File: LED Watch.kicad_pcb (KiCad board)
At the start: 2 copper layers, 41.9 x 49.3 mm, 140 parts, among them J1 AVR-ISP-6, J2 Lipo, J3 Coin Cell, SW1 SW_DPST, SW2 SW_DPST, U10 B39D3RGB-F6C0001HOU1930, U100 B39D3RGB-F6C0001HOU1930, U101 B39D3RGB-F6C0001HOU1930, U102 B39D3RGB-F6C0001HOU1930, U103 B39D3RGB-F6C0001HOU1930, U104 B39D3RGB-F6C0001HOU1930, U105 B39D3RGB-F6C0001HOU1930, U106 B39D3RGB-F6C0001HOU1930, U107 B39D3RGB-F6C0001HOU1930, U108 B39D3RGB-F6C0001HOU1930, U109 B39D3RGB-F6C0001HOU1930, U11 B39D3RGB-F6C0001HOU1930, U110 B39D3RGB-F6C0001HOU1930, U111 B39D3RGB-F6C0001HOU1930, U112 B39D3RGB-F6C0001HOU1930, U113 B39D3RGB-F6C0001HOU1930, U114 B39D3RGB-F6C0001HOU1930, U115 B39D3RGB-F6C0001HOU1930, U116 B39D3RGB-F6C0001HOU1930, U117 B39D3RGB-F6C0001HOU1930, U118 B39D3RGB-F6C0001HOU1930, U119 B39D3RGB-F6C0001HOU1930, U12 B39D3RGB-F6C0001HOU1930, U120 B39D3RGB-F6C0001HOU1930, U121 B39D3RGB-F6C0001HOU1930, U122 B39D3RGB-F6C0001HOU1930, U123 B39D3RGB-F6C0001HOU1930, U124 B39D3RGB-F6C0001HOU1930, U125 B39D3RGB-F6C0001HOU1930, U126 B39D3RGB-F6C0001HOU1930, U127 B39D3RGB-F6C0001HOU1930, U128 B39D3RGB-F6C0001HOU1930, U129 B39D3RGB-F6C0001HOU1930, U13 B39D3RGB-F6C0001HOU1930, U130 B39D3RGB-F6C0001HOU1930, U131 B39D3RGB-F6C0001HOU1930, U132 B39D3RGB-F6C0001HOU1930, U133 B39D3RGB-F6C0001HOU1930, U134 BMI160, U135 ATmega165PA-M, U14 B39D3RGB-F6C0001HOU1930, U15 B39D3RGB-F6C0001HOU1930, U16 B39D3RGB-F6C0001HOU1930, U17 B39D3RGB-F6C0001HOU1930, U18 B39D3RGB-F6C0001HOU1930, U19 B39D3RGB-F6C0001HOU1930, U2 B39D3RGB-F6C0001HOU1930, U20 B39D3RGB-F6C0001HOU1930, U21 B39D3RGB-F6C0001HOU1930, U22 B39D3RGB-F6C0001HOU1930, U23 B39D3RGB-F6C0001HOU1930, U24 B39D3RGB-F6C0001HOU1930, U25 B39D3RGB-F6C0001HOU1930, U26 B39D3RGB-F6C0001HOU1930, U27 B39D3RGB-F6C0001HOU1930, U28 B39D3RGB-F6C0001HOU1930, U29 B39D3RGB-F6C0001HOU1930, U3 B39D3RGB-F6C0001HOU1930, U30 B39D3RGB-F6C0001HOU1930, U31 B39D3RGB-F6C0001HOU1930, U32 B39D3RGB-F6C0001HOU1930, U33 B39D3RGB-F6C0001HOU1930, U34 B39D3RGB-F6C0001HOU1930, U35 B39D3RGB-F6C0001HOU1930, U36 B39D3RGB-F6C0001HOU1930, U37 B39D3RGB-F6C0001HOU1930, U38 B39D3RGB-F6C0001HOU1930, U39 B39D3RGB-F6C0001HOU1930, U4 B39D3RGB-F6C0001HOU1930, U40 B39D3RGB-F6C0001HOU1930, U41 B39D3RGB-F6C0001HOU1930, U42 B39D3RGB-F6C0001HOU1930, U43 B39D3RGB-F6C0001HOU1930, U44 B39D3RGB-F6C0001HOU1930, U45 B39D3RGB-F6C0001HOU1930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

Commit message: added caps.. still unsuccessful routing
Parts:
- added C1: C, Capacitor_SMD:C_0201_0603Metric, F.Cu at (99.2, 106.1)
- added C2: C, Capacitor_SMD:C_0201_0603Metric, F.Cu at (100.8, 106.1)
- moved Y1 0.20 mm to (100.0, 108.2)
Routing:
- net /G3: track 0.00 -> 199.2 mm, vias 0 -> 31
- net /G5: track 0.00 -> 194.5 mm, vias 0 -> 33
- net /G2: track 0.00 -> 190.8 mm, vias 0 -> 32
- net /G6: track 0.00 -> 187.2 mm, vias 0 -> 27
- net /G1: track 0.00 -> 182.5 mm, vias 0 -> 26
- net /G4: track 0.00 -> 176.7 mm, vias 0 -> 32
- net /R6: track 28.8 -> 203.0 mm, vias 0 -> 28
- net /B3: track 30.7 -> 203.0 mm, vias 0 -> 36
- net /R5: track 29.1 -> 200.8 mm, vias 0 -> 34
- net /B2: track 30.3 -> 201.3 mm, vias 0 -> 31
- net /B5: track 25.9 -> 187.7 mm, vias 0 -> 33
- net /R4: track 32.9 -> 193.0 mm, vias 0 -> 32
- net /R2: track 30.2 -> 187.7 mm, vias 0 -> 29
- net /B6: track 26.2 -> 183.1 mm, vias 0 -> 25
- net /B1: track 29.7 -> 179.1 mm, vias 0 -> 26
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- added copper zone on In1.Cu, net Net-(J1-GND)
- added copper zone on In2.Cu, net Net-(J1-VCC)
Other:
- board size 41.9 x 49.3 mm -> 42.9 x 50.3 mm
- copper layers 2 -> 4

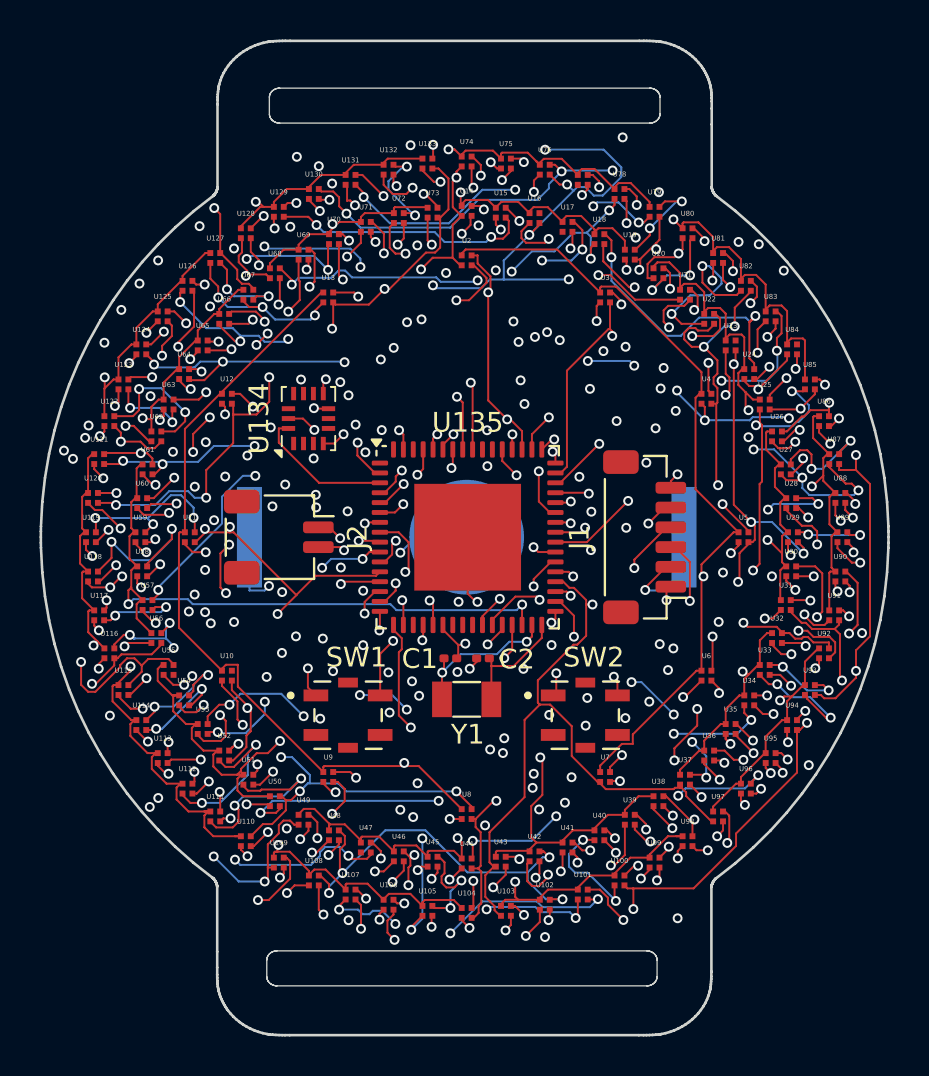
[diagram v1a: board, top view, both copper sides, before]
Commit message: traced out? iteration 1 at least.. passes an initial drc run.. I want to add a couple test regular white leds.. i should source and add for testing of potential single color board
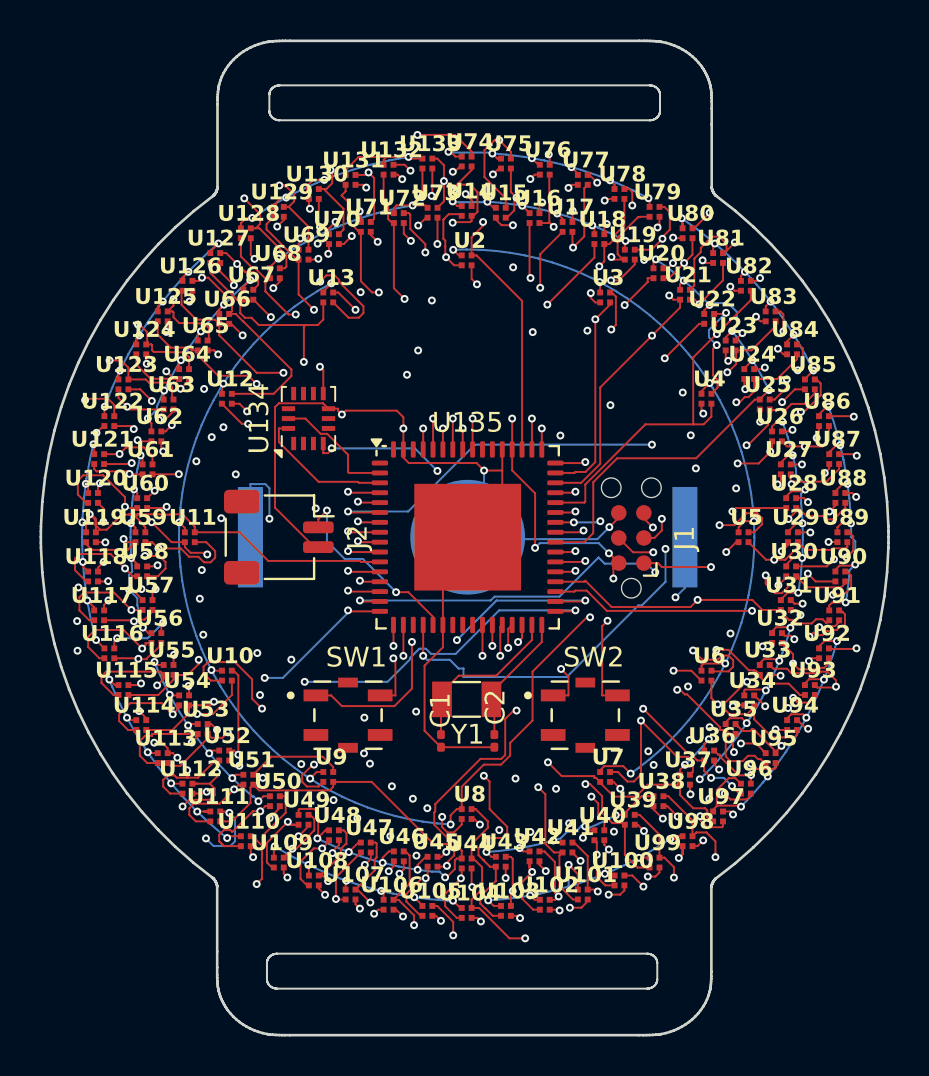
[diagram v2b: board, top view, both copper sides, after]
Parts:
- J1: footprint Connector_JST:JST_SH_BM06B-SRSS-TB_1x06-1MP_P1.00mm_Vertical -> Connector:Tag-Connect_TC2030-IDC-NL_2x03_P1.27mm_Vertical
- moved C2 4.21 mm to (101.4, 110.3), turned to -90 degrees
- moved C1 4.20 mm to (98.7, 110.3), turned to 90 degrees
- moved J1 0.67 mm to (108.3, 100.0)
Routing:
- net /R1: track 172.0 -> 208.5 mm, vias 29 -> 18
- net Net-(J1-GND): track 15.9 -> 49.6 mm, vias 9 -> 4
- net /R3: track 175.2 -> 208.3 mm, vias 30 -> 21
- net /G3: track 199.2 -> 166.8 mm, vias 31 -> 19
- net /B2: track 201.3 -> 178.0 mm, vias 31 -> 21
- net Net-(J1-VCC): track 14.5 -> 36.8 mm, vias 6 -> 9
- net /G6: track 187.2 -> 168.4 mm, vias 27 -> 24
- net /B3: track 203.0 -> 185.1 mm, vias 36 -> 25
- net /R2: track 187.7 -> 205.0 mm, vias 29 -> 19
- net /Second3: track 35.4 -> 51.9 mm, vias 2 -> 8
- net /G2: track 190.8 -> 174.8 mm, vias 32 -> 19
- net /G5: track 194.5 -> 178.9 mm, vias 33 -> 25
- net /G1: track 182.5 -> 167.8 mm, vias 26 -> 19
- net /Second5: track 36.7 -> 46.2 mm, vias 5 -> 7
- net /R4: track 193.0 -> 184.1 mm, vias 32 -> 16
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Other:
- outline, holes or cut-outs redrawn

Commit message: traced out, just a few minor cleanups.
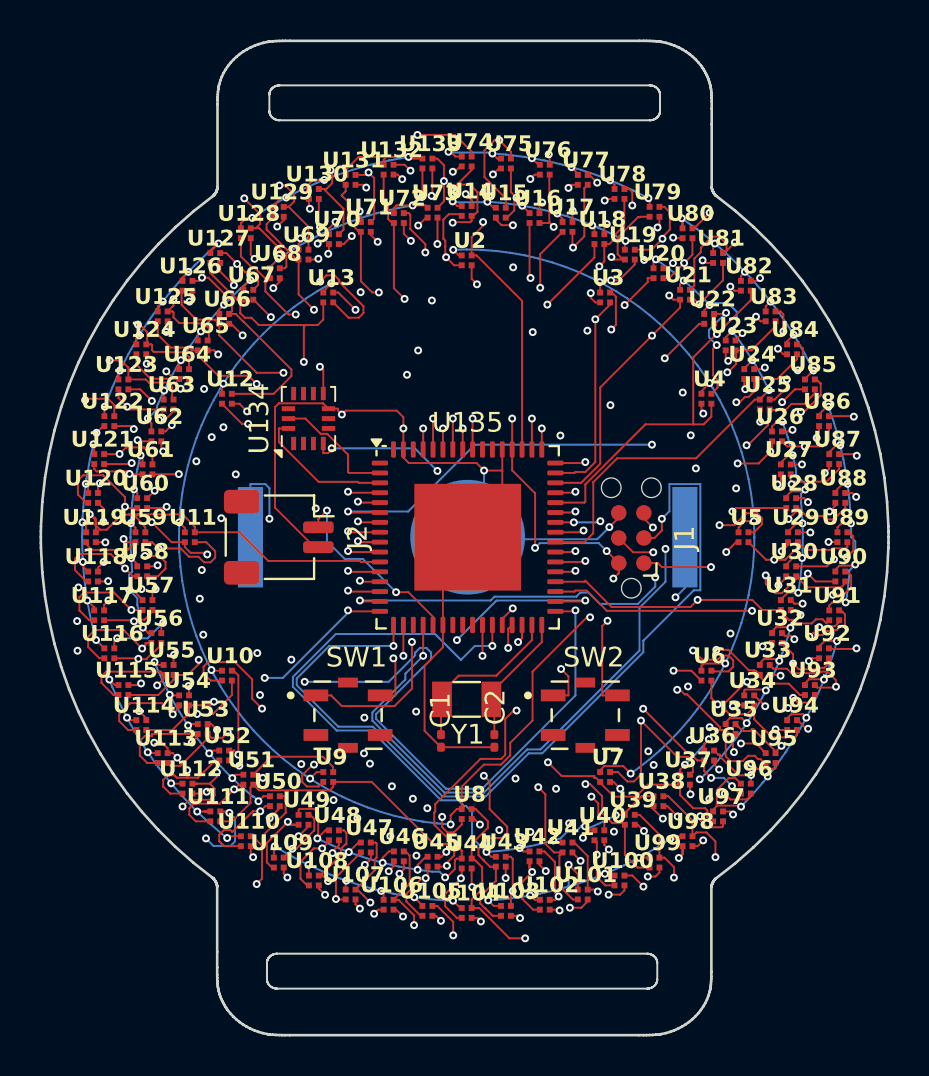
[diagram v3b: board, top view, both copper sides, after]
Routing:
- net /R6: track 207.8 -> 237.2 mm
- net /Minute5: track 23.8 -> 39.0 mm
- net /Second7: track 40.5 -> 54.6 mm
- net Net-(J1-~{RST}): track 20.2 -> 31.6 mm
- net /Minute6: track 29.5 -> 32.9 mm
- net Net-(U135-PF2): track 18.0 -> 19.4 mm
- net Net-(J1-GND): track 49.6 -> 48.3 mm
- net /Second5: track 46.2 -> 46.8 mm

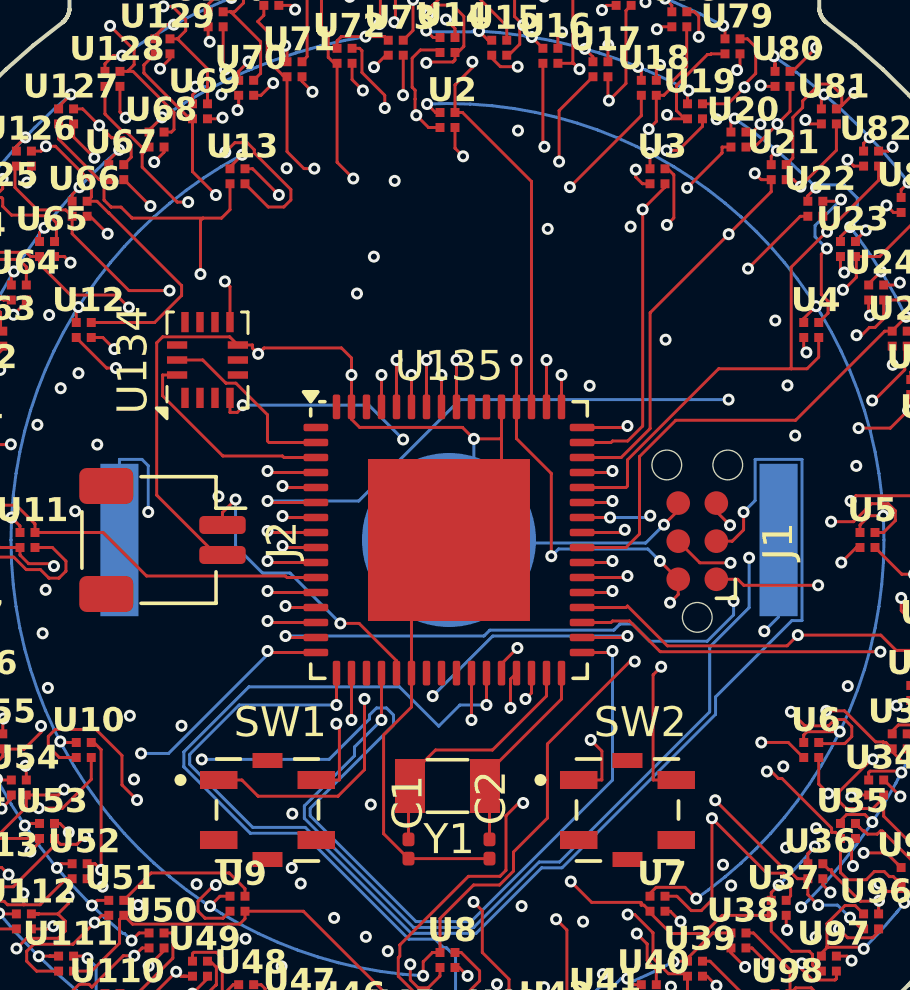
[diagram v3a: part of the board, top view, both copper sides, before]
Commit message: pulled vias from under chip and added 4 0603 pads for testing options
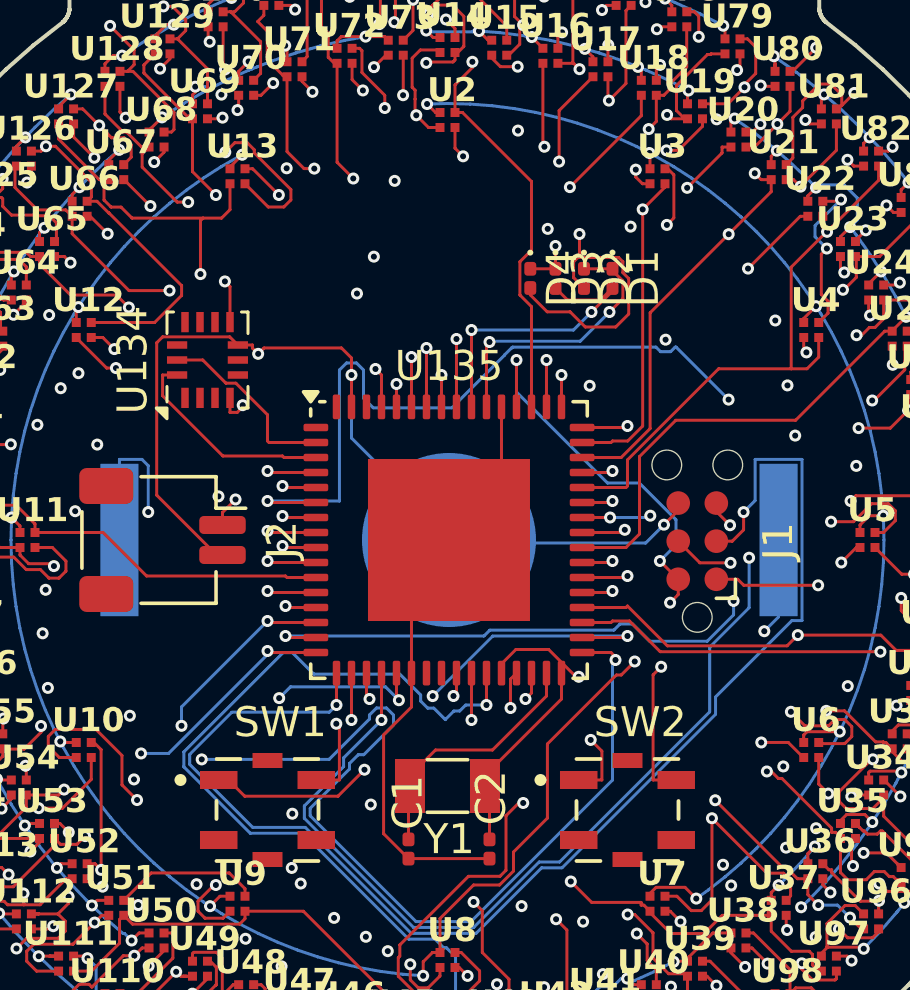
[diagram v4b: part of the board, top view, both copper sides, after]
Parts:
- added D1: LED, LED_SMD:LED_0201_0603Metric, F.Cu at (105.5, 91.3)
- added D2: LED, LED_SMD:LED_0201_0603Metric, F.Cu at (104.5, 91.3)
- added D3: LED, LED_SMD:LED_0201_0603Metric, F.Cu at (103.6, 91.3)
- added D4: LED, LED_SMD:LED_0201_0603Metric, F.Cu at (102.8, 91.3)
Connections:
- U135 pad 19: unconnected-(U135-PG4-Pad19) -> Net-(D3-K)
- U135 pad 25: unconnected-(U135-PD0-Pad25) -> Net-(D2-A)
- U135 pad 54: unconnected-(U135-PF7-Pad54) -> Net-(D1-K)
- U135 pad 55: unconnected-(U135-PF6-Pad55) -> Net-(D1-A)
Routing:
- net Net-(D2-A): track 0.00 -> 30.6 mm, vias 0 -> 2
- net Net-(D3-K): track 0.00 -> 24.9 mm, vias 0 -> 2
- net Net-(D1-A): track 0.00 -> 10.1 mm, vias 0 -> 2
- net Net-(D1-K): track 0.00 -> 9.34 mm, vias 0 -> 2
- net Net-(U134-INT1): track 18.7 -> 28.0 mm, vias 3 -> 2
- net Net-(J1-VCC): track 36.8 -> 42.8 mm
- net /Second3: track 51.9 -> 57.8 mm
- net Net-(U135-PF1): track 17.9 -> 20.4 mm
- net Net-(J1-GND): track 48.3 -> 46.9 mm, vias 4 -> 3
- net Net-(U135-PF2): track 19.4 -> 20.7 mm
- net Net-(U135-PF3): track 20.8 -> 22.1 mm
- net /Minute8: track 34.3 -> 33.3 mm
- net Net-(U135-PF0): track 19.9 -> 20.8 mm
- net /Minute5: track 39.0 -> 39.9 mm
- net /Second5: track 46.8 -> 47.6 mm
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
